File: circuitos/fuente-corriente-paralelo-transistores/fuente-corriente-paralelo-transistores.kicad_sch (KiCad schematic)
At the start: 17 parts, among them J2 Conn_01x04_Pin, J3 Conn_01x04_Pin, Q1 BC548, Q2 BC548, Q3 BC548, U1 LM324, U2 Pico

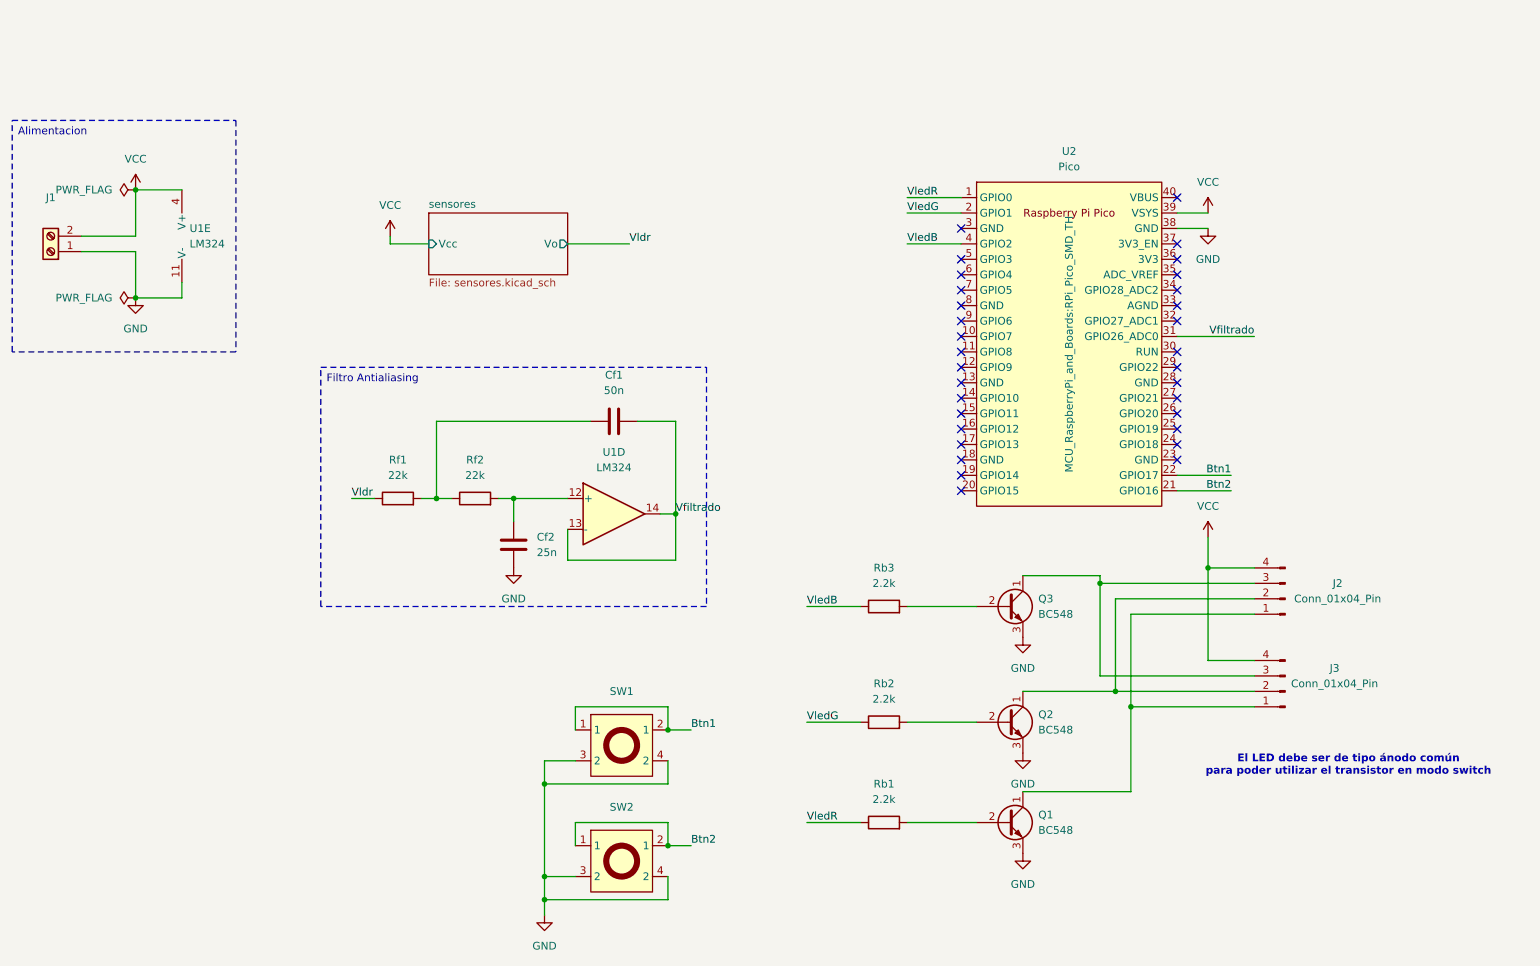
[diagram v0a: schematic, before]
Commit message: pcb con LDRs y led ws2812b-mini
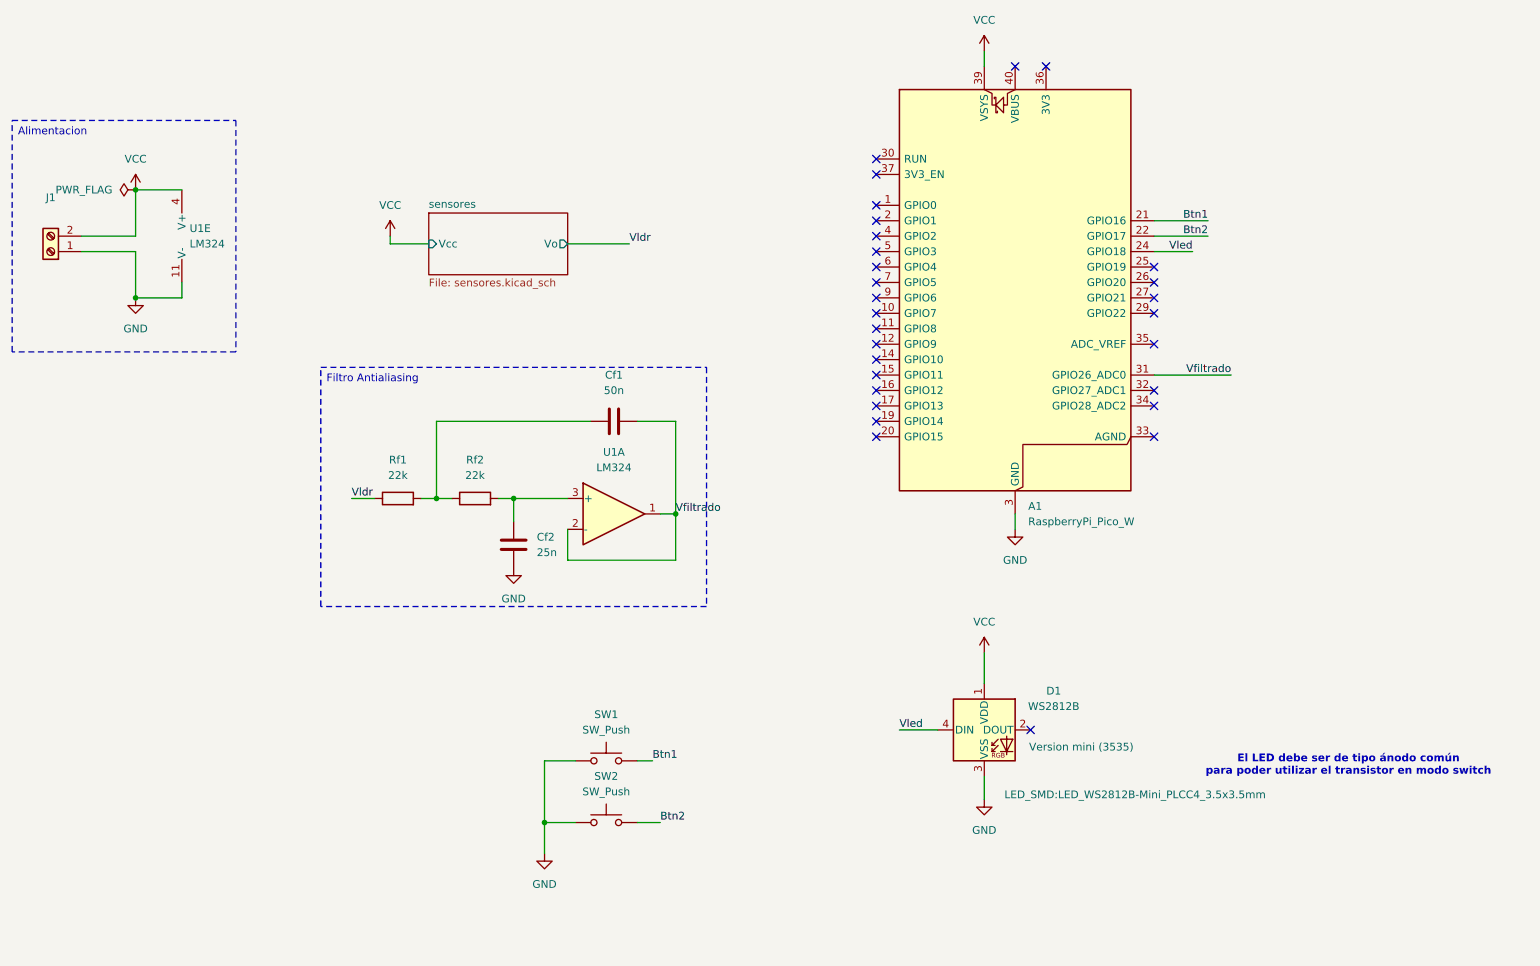
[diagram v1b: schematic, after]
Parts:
- removed J2, J3: Conn_01x04_Pin, Connector_PinHeader_2.54mm:PinHeader_1x04_P2.54mm_Vertical, symbol Connector:Conn_01x04_Pin
- removed Q1, Q2, Q3: BC548, Package_TO_SOT_THT:TO-92_Inline, symbol Transistor_BJT:BC548
- removed Rb1, Rb2, Rb3: 2.2k, symbol Device:R
- removed SW1, SW2: ~, Button_Switch_THT:SW_PUSH-12mm, symbol mariano:push_button
- removed U2: Pico, MCU_RaspberryPi_and_Boards:RPi_Pico_SMD_TH, symbol MCU_RaspberryPi_and_Boards:Pico
- added A1: RaspberryPi_Pico_W, Module:RaspberryPi_Pico_Common_THT, symbol MCU_Module:RaspberryPi_Pico_W
- added D1: WS2812B, LED_SMD:LED_WS2812B-Mini_PLCC4_3.5x3.5mm, symbol LED:WS2812B
- added SW1, SW2: SW_Push, Button_Switch_THT:SW_PUSH-12mm, symbol Switch:SW_Push
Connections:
- net Btn1: now also A1.21 (GPIO16), SW1.2
- net Btn2: now also A1.22 (GPIO17), SW2.2
- net GND: now also A1.13 (GND), A1.18 (GND), A1.23 (GND), A1.28 (GND), A1.3 (GND), A1.38 (GND), A1.8 (GND), D1.3 (VSS), SW1.1, SW2.1
- net VCC: now also A1.39 (VSYS), D1.1 (VDD)
- net Vfiltrado: now also U1.1, U1.2 (-), A1.31 (GPIO26_ADC0); no longer U1.13 (-), U1.14
- net at Cf2.1, Rf2.2: now also U1.3 (+); no longer U1.12 (+)
- new net Vled: A1.24 (GPIO18), D1.4 (DIN)
- no-connect marks 32 -> 29
